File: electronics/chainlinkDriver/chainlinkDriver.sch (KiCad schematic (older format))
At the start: 65 parts, among them J10 Sensor C, J11 Sensor D, J12 Motor E, J13 Motor F, J14 Sensor E, J15 Sensor F, J16 Power, J17 Power, J18 Power, J19 Input, J20 Output, J3 Motor A, J5 Motor B, J6 Motor C, J7 Motor D, J8 Sensor A, J9 Sensor B, U1 74HC595, U10 TPL7407L, U2 TPL7407L, U3 74HC125, U4 74HC165, U5 74HC595, U6 TPL7407L, U7 74HC595, U8 TPL7407L, U9 74HC595

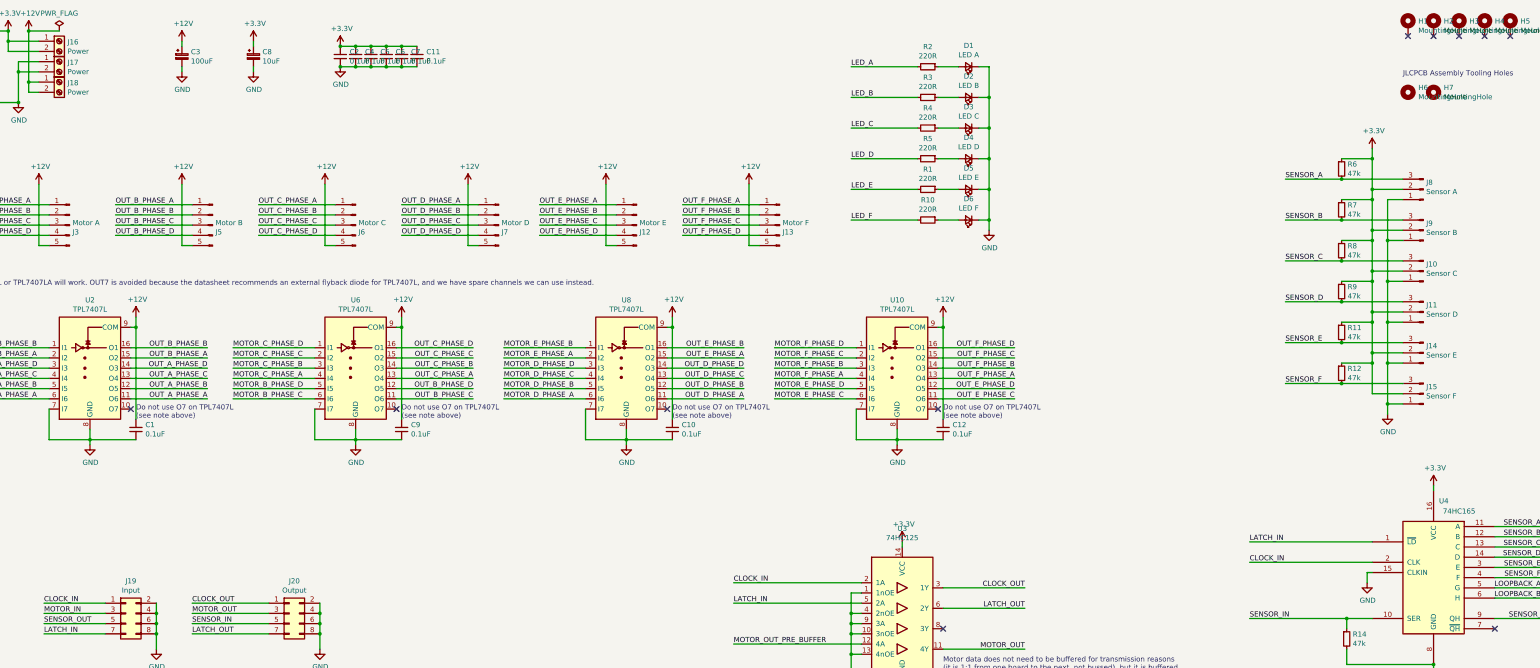
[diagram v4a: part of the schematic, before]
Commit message: Update values so LEDs, connectors can be grouped in BOM; add some LCSC alternative part numbers
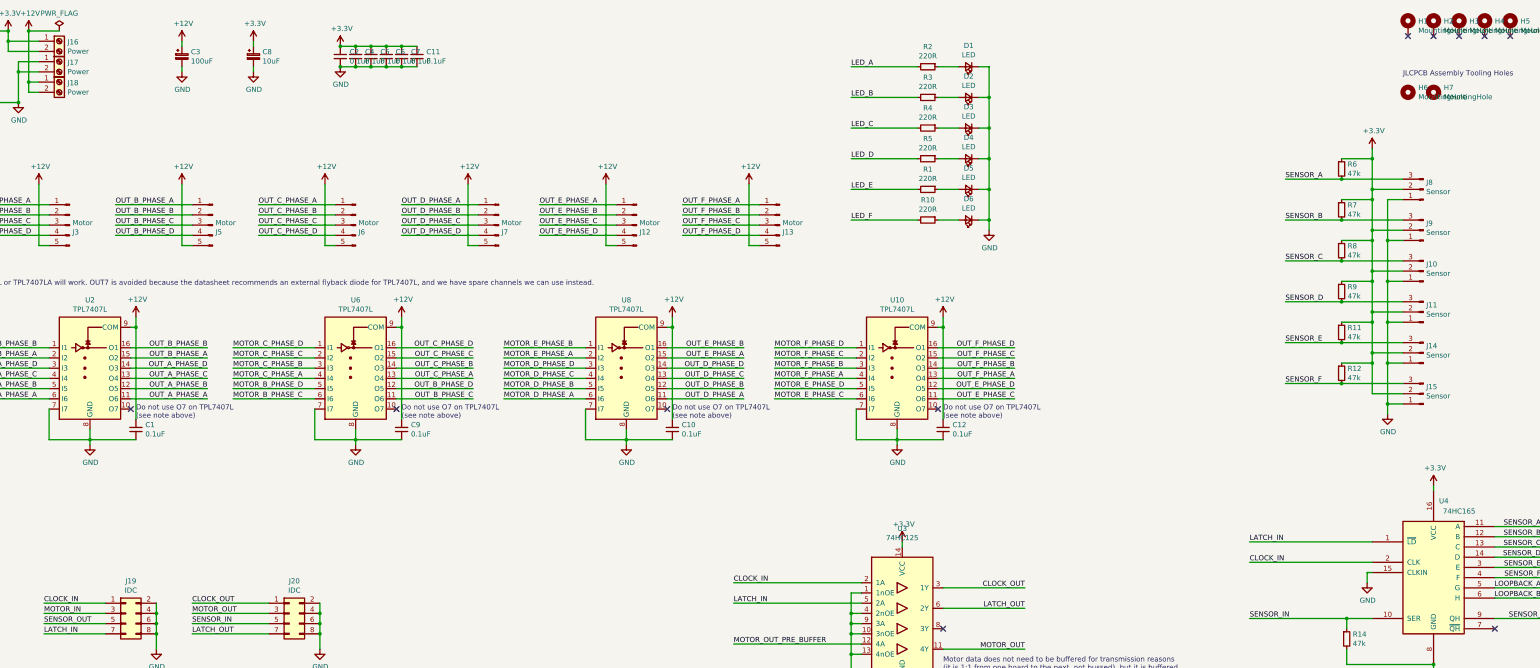
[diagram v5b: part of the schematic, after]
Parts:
- C8: LCSC_ALT_3V3_CAP (none) -> C176661
- D1: value LED A -> LED; LCSC_ALT_LED (none) -> C72044
- D2: value LED B -> LED; LCSC_ALT_LED (none) -> C72044
- D3: value LED C -> LED; LCSC_ALT_LED (none) -> C72044
- D4: value LED D -> LED; LCSC_ALT_LED (none) -> C72044
- D5: value LED E -> LED; LCSC_ALT_LED (none) -> C72044
- D6: value LED F -> LED; LCSC_ALT_LED (none) -> C72044
- J10: value Sensor C -> Sensor
- J11: value Sensor D -> Sensor
- J12: value Motor E -> Motor
- J13: value Motor F -> Motor
- J14: value Sensor E -> Sensor
- J15: value Sensor F -> Sensor
- J19: value Input -> IDC
- J20: value Output -> IDC
- J3: value Motor A -> Motor
- J5: value Motor B -> Motor
- J6: value Motor C -> Motor
- J7: value Motor D -> Motor
- J8: value Sensor A -> Sensor
- J9: value Sensor B -> Sensor
- U3: LCSC_ALT_BUFFER (none) -> C7390
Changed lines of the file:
@@
 P 1700 2700
 F 0 "J3" H 1672 2632 50  0000 R CNN
-F 1 "Motor A" H 1672 2723 50  0000 R CNN
+F 1 "Motor" H 1672 2723 50  0000 R CNN
 F 2 "Connector_JST:JST_XH_B5B-XH-A_1x05_P2.50mm_Vertical" H 1700 2700 50  0001 C CNN
 F 3 "~" H 1700 2700 50  0001 C CNN
@@
 P 3100 2700
 F 0 "J5" H 3072 2632 50  0000 R CNN
-F 1 "Motor B" H 3072 2723 50  0000 R CNN
+F 1 "Motor" H 3072 2723 50  0000 R CNN
 F 2 "Connector_JST:JST_XH_B5B-XH-A_1x05_P2.50mm_Vertical" H 3100 2700 50  0001 C CNN
 F 3 "~" H 3100 2700 50  0001 C CNN
@@
 P 4500 2700
 F 0 "J6" H 4472 2632 50  0000 R CNN
-F 1 "Motor C" H 4472 2723 50  0000 R CNN
+F 1 "Motor" H 4472 2723 50  0000 R CNN
 F 2 "Connector_JST:JST_XH_B5B-XH-A_1x05_P2.50mm_Vertical" H 4500 2700 50  0001 C CNN
 F 3 "~" H 4500 2700 50  0001 C CNN
@@
 P 5900 2700
 F 0 "J7" H 5872 2632 50  0000 R CNN
-F 1 "Motor D" H 5872 2723 50  0000 R CNN
+F 1 "Motor" H 5872 2723 50  0000 R CNN
 F 2 "Connector_JST:JST_XH_B5B-XH-A_1x05_P2.50mm_Vertical" H 5900 2700 50  0001 C CNN
 F 3 "~" H 5900 2700 50  0001 C CNN
@@
 F 4 "C134721" H 3500 1050 50  0001 C CNN "LCSC"
 F 5 "0;0;180" H 3500 1050 50  0001 C CNN "JLCPCB_CORRECTION"
+F 6 "C176661" H 3500 1050 50  0001 C CNN "LCSC_ALT_3V3_CAP"
 	1    3500 1050
 	1    0    0    -1
@@
 P 10500 1150
 F 0 "D1" H 10500 943 50  0000 C CNN
-F 1 "LED A" H 10500 1034 50  0000 C CNN
+F 1 "LED" H 10500 1034 50  0000 C CNN
 F 2 "ModifiedSymbols:LED_0603_1608Metric_Silkscreen" V 10500 1150 50  0001 C CNN
 F 3 "~" V 10500 1150 50  0001 C CNN
 F 4 "C2286" H 10500 1150 50  0001 C CNN "LCSC"
+F 5 "C72044" H 10500 1150 50  0001 C CNN "LCSC_ALT_LED"
 	1    10500 1150
 	-1   0    0    1
@@
 P 10500 1450
 F 0 "D2" H 10500 1243 50  0000 C CNN
-F 1 "LED B" H 10500 1334 50  0000 C CNN
+F 1 "LED" H 10500 1334 50  0000 C CNN
 F 2 "ModifiedSymbols:LED_0603_1608Metric_Silkscreen" V 10500 1450 50  0001 C CNN
 F 3 "~" V 10500 1450 50  0001 C CNN
 F 4 "C2286" H 10500 1450 50  0001 C CNN "LCSC"
+F 5 "C72044" H 10500 1450 50  0001 C CNN "LCSC_ALT_LED"
 	1    10500 1450
 	-1   0    0    1
@@
 P 10500 1750
 F 0 "D3" H 10500 1543 50  0000 C CNN
-F 1 "LED C" H 10500 1634 50  0000 C CNN
+F 1 "LED" H 10500 1634 50  0000 C CNN
 F 2 "ModifiedSymbols:LED_0603_1608Metric_Silkscreen" V 10500 1750 50  0001 C CNN
 F 3 "~" V 10500 1750 50  0001 C CNN
 F 4 "C2286" H 10500 1750 50  0001 C CNN "LCSC"
+F 5 "C72044" H 10500 1750 50  0001 C CNN "LCSC_ALT_LED"
 	1    10500 1750
 	-1   0    0    1
@@
 P 10500 2050
 F 0 "D4" H 10500 1843 50  0000 C CNN
-F 1 "LED D" H 10500 1934 50  0000 C CNN
+F 1 "LED" H 10500 1934 50  0000 C CNN
 F 2 "ModifiedSymbols:LED_0603_1608Metric_Silkscreen" V 10500 2050 50  0001 C CNN
 F 3 "~" V 10500 2050 50  0001 C CNN
 F 4 "C2286" H 10500 2050 50  0001 C CNN "LCSC"
+F 5 "C72044" H 10500 2050 50  0001 C CNN "LCSC_ALT_LED"
 	1    10500 2050
 	-1   0    0    1
@@
 P 14950 2350
 F 0 "J8" H 14922 2282 50  0000 R CNN
-F 1 "Sensor A" H 14922 2373 50  0000 R CNN
+F 1 "Sensor" H 14922 2373 50  0000 R CNN
 F 2 "Connector_PinHeader_2.54mm:PinHeader_1x03_P2.54mm_Vertical" H 14950 2350 50  0001 C CNN
 F 3 "~" H 14950 2350 50  0001 C CNN
@@
 P 14950 2750
 F 0 "J9" H 14922 2682 50  0000 R CNN
-F 1 "Sensor B" H 14922 2773 50  0000 R CNN
+F 1 "Sensor" H 14922 2773 50  0000 R CNN
 F 2 "Connector_PinHeader_2.54mm:PinHeader_1x03_P2.54mm_Vertical" H 14950 2750 50  0001 C CNN
 F 3 "~" H 14950 2750 50  0001 C CNN
@@
 P 14950 3150
 F 0 "J10" H 14922 3082 50  0000 R CNN
-F 1 "Sensor C" H 14922 3173 50  0000 R CNN
+F 1 "Sensor" H 14922 3173 50  0000 R CNN
 F 2 "Connector_PinHeader_2.54mm:PinHeader_1x03_P2.54mm_Vertical" H 14950 3150 50  0001 C CNN
 F 3 "~" H 14950 3150 50  0001 C CNN
@@
 P 14950 3550
 F 0 "J11" H 14922 3482 50  0000 R CNN
-F 1 "Sensor D" H 14922 3573 50  0000 R CNN
+F 1 "Sensor" H 14922 3573 50  0000 R CNN
 F 2 "Connector_PinHeader_2.54mm:PinHeader_1x03_P2.54mm_Vertical" H 14950 3550 50  0001 C CNN
 F 3 "~" H 14950 3550 50  0001 C CNN
@@
 P 7250 2700
 F 0 "J12" H 7222 2632 50  0000 R CNN
-F 1 "Motor E" H 7222 2723 50  0000 R CNN
+F 1 "Motor" H 7222 2723 50  0000 R CNN
 F 2 "Connector_JST:JST_XH_B5B-XH-A_1x05_P2.50mm_Vertical" H 7250 2700 50  0001 C CNN
 F 3 "~" H 7250 2700 50  0001 C CNN
@@
 P 8650 2700
 F 0 "J13" H 8622 2632 50  0000 R CNN
-F 1 "Motor F" H 8622 2723 50  0000 R CNN
+F 1 "Motor" H 8622 2723 50  0000 R CNN
 F 2 "Connector_JST:JST_XH_B5B-XH-A_1x05_P2.50mm_Vertical" H 8650 2700 50  0001 C CNN
 F 3 "~" H 8650 2700 50  0001 C CNN
@@
 P 10500 2350
 F 0 "D5" H 10500 2143 50  0000 C CNN
-F 1 "LED E" H 10500 2234 50  0000 C CNN
+F 1 "LED" H 10500 2234 50  0000 C CNN
 F 2 "ModifiedSymbols:LED_0603_1608Metric_Silkscreen" V 10500 2350 50  0001 C CNN
 F 3 "~" V 10500 2350 50  0001 C CNN
 F 4 "C2286" H 10500 2350 50  0001 C CNN "LCSC"
+F 5 "C72044" H 10500 2350 50  0001 C CNN "LCSC_ALT_LED"
 	1    10500 2350
 	-1   0    0    1
@@
 P 10500 2650
 F 0 "D6" H 10500 2443 50  0000 C CNN
-F 1 "LED F" H 10500 2534 50  0000 C CNN
+F 1 "LED" H 10500 2534 50  0000 C CNN
 F 2 "ModifiedSymbols:LED_0603_1608Metric_Silkscreen" V 10500 2650 50  0001 C CNN
 F 3 "~" V 10500 2650 50  0001 C CNN
 F 4 "C2286" H 10500 2650 50  0001 C CNN "LCSC"
+F 5 "C72044" H 10500 2650 50  0001 C CNN "LCSC_ALT_LED"
 	1    10500 2650
 	-1   0    0    1
@@
 P 14950 3950
 F 0 "J14" H 14922 3882 50  0000 R CNN
-F 1 "Sensor E" H 14922 3973 50  0000 R CNN
+F 1 "Sensor" H 14922 3973 50  0000 R CNN
 F 2 "Connector_PinHeader_2.54mm:PinHeader_1x03_P2.54mm_Vertical" H 14950 3950 50  0001 C CNN
 F 3 "~" H 14950 3950 50  0001 C CNN
@@
 P 14950 4350
 F 0 "J15" H 14922 4282 50  0000 R CNN
-F 1 "Sensor F" H 14922 4373 50  0000 R CNN
+F 1 "Sensor" H 14922 4373 50  0000 R CNN
 F 2 "Connector_PinHeader_2.54mm:PinHeader_1x03_P2.54mm_Vertical" H 14950 4350 50  0001 C CNN
 F 3 "~" H 14950 4350 50  0001 C CNN
@@
 F 4 "C5598" H 9850 6550 50  0001 C CNN "LCSC"
 F 5 "0;0;-90" H 9850 6550 50  0001 C CNN "JLCPCB_CORRECTION"
+F 6 "C7390" H 9850 6550 50  0001 C CNN "LCSC_ALT_BUFFER"
 	1    9850 6550
 	1    0    0    -1
@@
 P 2250 6500
 F 0 "J19" H 2300 6817 50  0000 C CNN
-F 1 "Input" H 2300 6726 50  0000 C CNN
+F 1 "IDC" H 2300 6726 50  0000 C CNN
 F 2 "ModifiedSymbols:IDC-Header_2x04_P2.54mm_Vertical" H 2250 6500 50  0001 C CNN
 F 3 "~" H 2250 6500 50  0001 C CNN
@@
 P 3850 6500
 F 0 "J20" H 3900 6817 50  0000 C CNN
-F 1 "Output" H 3900 6726 50  0000 C CNN
+F 1 "IDC" H 3900 6726 50  0000 C CNN
 F 2 "ModifiedSymbols:IDC-Header_2x04_P2.54mm_Vertical" H 3850 6500 50  0001 C CNN
 F 3 "~" H 3850 6500 50  0001 C CNN

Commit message: Add alternative part numbers for 3.3v capacitor and 74HC125
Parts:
- U3: LCSC_ALT_BUFFER2 (none) -> C94424
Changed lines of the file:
@@
-$EndComp
-$Comp
-L Device:CP_Small C8
-U 1 1 60F56FCC
-P 3500 1050
-F 0 "C8" H 3588 1096 50  0000 L CNN
-F 1 "10uF" H 3588 1005 50  0000 L CNN
-F 2 "Capacitor_SMD:CP_Elec_4x5.3" H 3500 1050 50  0001 C CNN
-F 3 "~" H 3500 1050 50  0001 C CNN
-F 4 "C134721" H 3500 1050 50  0001 C CNN "LCSC"
-F 5 "0;0;180" H 3500 1050 50  0001 C CNN "JLCPCB_CORRECTION"
-F 6 "C176661" H 3500 1050 50  0001 C CNN "LCSC_ALT_3V3_CAP"
-	1    3500 1050
-	1    0    0    -1
 $EndComp
 $Comp
@@
 F 5 "0;0;-90" H 9850 6550 50  0001 C CNN "JLCPCB_CORRECTION"
 F 6 "C7390" H 9850 6550 50  0001 C CNN "LCSC_ALT_BUFFER"
+F 7 "C94424" H 9850 6550 50  0001 C CNN "LCSC_ALT_BUFFER2"
 	1    9850 6550
 	1    0    0    -1
@@
 Text Label 13250 5800 0    50   ~ 0
 LATCH_IN
+$Comp
+L Device:CP_Small C8
+U 1 1 60F56FCC
+P 3500 1050
+F 0 "C8" H 3588 1096 50  0000 L CNN
+F 1 "10uF" H 3588 1005 50  0000 L CNN
+F 2 "Capacitor_SMD:CP_Elec_4x5.3" H 3500 1050 50  0001 C CNN
+F 3 "~" H 3500 1050 50  0001 C CNN
+F 4 "C134721" H 3500 1050 50  0001 C CNN "LCSC"
+F 5 "0;0;180" H 3500 1050 50  0001 C CNN "JLCPCB_CORRECTION"
+F 6 "C176661" H 3500 1050 50  0001 C CNN "LCSC_ALT_3V3_CAP"
+	1    3500 1050
+	1    0    0    -1
+$EndComp
 $EndSCHEMATC

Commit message: Output enable ChainlinkDriver
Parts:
- added R13: 47k, Resistor_SMD:R_0603_1608Metric, symbol Device:R_Small
- J19, J20: footprint ModifiedSymbols:IDC-Header_2x04_P2.54mm_Vertical -> ModifiedSymbols:IDC-Header_2x05_P2.54mm_Vertical_2x04Silk; symbol Connector_Generic:Conn_02x04_Odd_Even -> Connector_Generic:Conn_02x05_Odd_Even
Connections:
- net +3V3: now also R13.1
- net GND: now also J19.10 (Pin_10), J20.10 (Pin_10); no longer U1.13 (~OE), U3.9 (3A), U5.13 (~OE), U7.13 (~OE), U9.13 (~OE)
- net nOE_OUT: now reaches U3.8 (3Y)
- net nOE_OUT: now also J20.9 (Pin_9)
- new net nOE_IN: J19.9 (Pin_9), R13.2, U1.13 (~OE), U3.9 (3A), U5.13 (~OE), U7.13 (~OE), U9.13 (~OE)
- no-connect marks 11 -> 10
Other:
- note added: "TPL7407L or TPL7407LA will work. OUT7 is avoided because the datasheet recommends an external flyback diode for TPL7407L, and we have spare channels we can use instead.\nULN2003A is an acceptable replacement, but less efficient."
- note removed: "TPL7407L or TPL7407LA will work. OUT7 is avoided because the datasheet recommends an external flyback diode for TPL7407L, and we have spare channels we can use instead."
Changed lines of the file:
@@
 	1750 8400 2200 8400
 Connection ~ 2200 8400
-Wire Wire Line
-	1800 9100 1150 9100
-Text Label 1150 9100 0    50   ~ 0
-LATCH_IN
 $Comp
 L power:GND #PWR08
@@
 Wire Wire Line
 	13250 6000 14450 6000
-Wire Wire Line
-	1800 9200 1750 9200
-Wire Wire Line
-	1750 9200 1750 9750
-Wire Wire Line
-	1750 9750 2200 9750
-Connection ~ 2200 9750
-Wire Wire Line
-	4250 9200 4200 9200
-Wire Wire Line
-	4200 9200 4200 9750
-Wire Wire Line
-	4200 9750 4650 9750
-Connection ~ 4650 9750
-Wire Wire Line
-	9150 9200 9100 9200
-Wire Wire Line
-	9100 9200 9100 9750
-Wire Wire Line
-	9100 9750 9550 9750
-Connection ~ 9550 9750
 $Comp
 L Device:R_Small R6
@@
 	1    0    0    -1
 $EndComp
-Wire Wire Line
-	6700 9200 6650 9200
-Wire Wire Line
-	6650 9200 6650 9750
-Wire Wire Line
-	6650 9750 7100 9750
-Connection ~ 7100 9750
 Wire Wire Line
 	7500 8800 8350 8800
@@
 JLCPCB Assembly Tooling Holes
 Text Notes 700  3300 0    50   ~ 0
-TPL7407L or TPL7407LA will work. OUT7 is avoided because the datasheet recommends an external flyback diode for TPL7407L, and we have spare channels we can use instead.
+TPL7407L or TPL7407LA will work. OUT7 is avoided because the datasheet recommends an external flyback diode for TPL7407L, and we have spare channels we can use instead.\nULN2003A is an acceptable replacement, but less efficient.
 Text Notes 2350 4600 0    50   ~ 0
 Do not use O7 on TPL7407L\n(see note above)
@@
 	1450 6400 2050 6400
 $Comp
-L Connector_Generic:Conn_02x04_Odd_Even J19
+L Connector_Generic:Conn_02x05_Odd_Even J19
 U 1 1 61861E9F
-P 2250 6500
-F 0 "J19" H 2300 6817 50  0000 C CNN
-F 1 "IDC" H 2300 6726 50  0000 C CNN
-F 2 "ModifiedSymbols:IDC-Header_2x04_P2.54mm_Vertical" H 2250 6500 50  0001 C CNN
-F 3 "~" H 2250 6500 50  0001 C CNN
-	1    2250 6500
+P 2250 6600
+F 0 "J19" H 2300 6917 50  0000 C CNN
+F 1 "IDC" H 2300 6826 50  0000 C CNN
+F 2 "ModifiedSymbols:IDC-Header_2x05_P2.54mm_Vertical_2x04Silk" H 2250 6600 50  0001 C CNN
+F 3 "~" H 2250 6600 50  0001 C CNN
+	1    2250 6600
 	1    0    0    -1
 $EndComp
@@
 Connection ~ 2550 6700
 Wire Wire Line
-	2550 6700 2550 6850
-$Comp
-L Connector_Generic:Conn_02x04_Odd_Even J20
+	2550 6700 2550 6800
+$Comp
+L Connector_Generic:Conn_02x05_Odd_Even J20
 U 1 1 618D5E87
-P 3850 6500
-F 0 "J20" H 3900 6817 50  0000 C CNN
-F 1 "IDC" H 3900 6726 50  0000 C CNN
-F 2 "ModifiedSymbols:IDC-Header_2x04_P2.54mm_Vertical" H 3850 6500 50  0001 C CNN
-F 3 "~" H 3850 6500 50  0001 C CNN
-	1    3850 6500
-	1    0    0    -1
-$EndComp
-Wire Wire Line
-	4150 6850 4150 6700
+P 3850 6600
+F 0 "J20" H 3900 6917 50  0000 C CNN
+F 1 "IDC" H 3900 6826 50  0000 C CNN
+F 2 "ModifiedSymbols:IDC-Header_2x05_P2.54mm_Vertical_2x04Silk" H 3850 6600 50  0001 C CNN
+F 3 "~" H 3850 6600 50  0001 C CNN
+	1    3850 6600
+	1    0    0    -1
+$EndComp
+Wire Wire Line
+	4150 6850 4150 6800
 Connection ~ 4150 6500
 Wire Wire Line
@@
 Wire Wire Line
 	4150 6600 4150 6500
-Connection ~ 4150 6700
 Wire Wire Line
 	4150 6700 4150 6600
@@
 Text Label 11050 6450 2    50   ~ 0
 LATCH_OUT
-NoConn ~ 10250 6650
-Wire Wire Line
-	9450 6600 9350 6600
-Wire Wire Line
-	9350 6500 9350 6600
-Wire Wire Line
-	9350 6600 9350 6700
-Connection ~ 9350 6600
 Text Label 13250 5800 0    50   ~ 0
 LATCH_IN
@@
 	1    0    0    -1
 $EndComp
+Wire Wire Line
+	9350 6500 9350 6700
+Wire Wire Line
+	8200 6600 9450 6600
+Text Label 8200 6600 0    50   ~ 0
+nOE_IN
+Wire Wire Line
+	10250 6650 11050 6650
+Text Label 11050 6650 2    50   ~ 0
+nOE_OUT
+Text Label 1150 9100 0    50   ~ 0
+LATCH_IN
+Wire Wire Line
+	1800 9100 1150 9100
+Text Label 1150 9200 0    50   ~ 0
+nOE_IN
+Wire Wire Line
+	1800 9200 1150 9200
+Text Label 3600 9200 0    50   ~ 0
+nOE_IN
+Wire Wire Line
+	4250 9200 3600 9200
+Text Label 6050 9200 0    50   ~ 0
+nOE_IN
+Wire Wire Line
+	6700 9200 6050 9200
+Text Label 8500 9200 0    50   ~ 0
+nOE_IN
+Wire Wire Line
+	9150 9200 8500 9200
+Text Label 5350 6700 0    50   ~ 0
+nOE_IN
+Wire Wire Line
+	6000 6700 5350 6700
+$Comp
+L power:+3.3V #PWR0101
+U 1 1 634A3C40
+P 6000 6200
+F 0 "#PWR0101" H 6000 6050 50  0001 C CNN
+F 1 "+3.3V" H 6015 6373 50  0000 C CNN
+F 2 "" H 6000 6200 50  0001 C CNN
+F 3 "" H 6000 6200 50  0001 C CNN
+	1    6000 6200
+	1    0    0    -1
+$EndComp
+Wire Wire Line
+	6000 6350 6000 6200
+Wire Wire Line
+	6000 6700 6000 6550
+$Comp
+L Device:R_Small R13
+U 1 1 6352DF17
+P 6000 6450
+F 0 "R13" H 6059 6496 50  0000 L CNN
+F 1 "47k" H 6059 6405 50  0000 L CNN
+F 2 "Resistor_SMD:R_0603_1608Metric" H 6000 6450 50  0001 C CNN
+F 3 "~" H 6000 6450 50  0001 C CNN
+F 4 "C25819" H 6000 6450 50  0001 C CNN "LCSC"
+	1    6000 6450
+	1    0    0    -1
+$EndComp
+Wire Wire Line
+	2550 6850 2550 6800
+Connection ~ 2550 6800
+Wire Wire Line
+	4150 6800 4150 6700
+Connection ~ 4150 6800
+Connection ~ 4150 6700
+Text Label 1450 6800 0    50   ~ 0
+nOE_IN
+Wire Wire Line
+	1450 6800 2050 6800
+Text Label 2900 6800 0    50   ~ 0
+nOE_OUT
+Wire Wire Line
+	2900 6800 3650 6800
 $EndSCHEMATC
